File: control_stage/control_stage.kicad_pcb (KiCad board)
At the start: 2 copper layers, 100 x 80 mm, 108 parts, among them J1 DB9, J2 DB15, P1 CONN_01X04, P2 CONN_01X04, P3 CONN_01X04, P4 CONN_01X04, P8 CONN_01X01, U1 XMC4400-F100, U14 AD8226, U15 MAX3463, U18 LT1764EQ, U19 KSZ8081, U2 ips511g, U20 ETH100_MAG, U21 MAX3463, U22 MAX3463, U23 MAX3463, U3 ips511g, U4 MAX3463, U5 AD8226, U6 LT1764EQ, X1 NKE1212DC, Y1 12MHz, Y2 25MHz

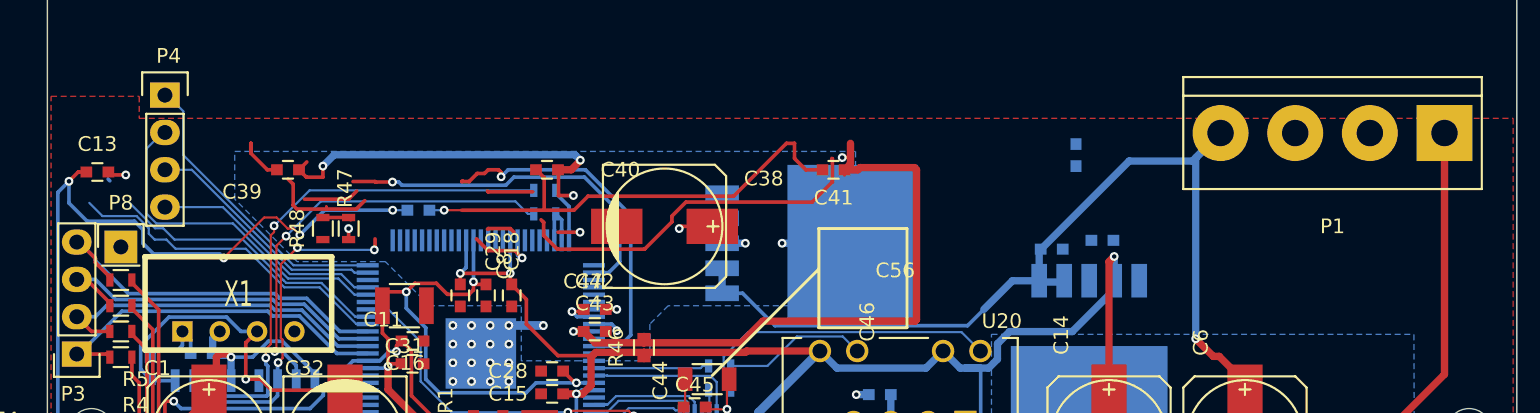
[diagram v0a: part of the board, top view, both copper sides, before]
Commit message: Control stage, initial version.
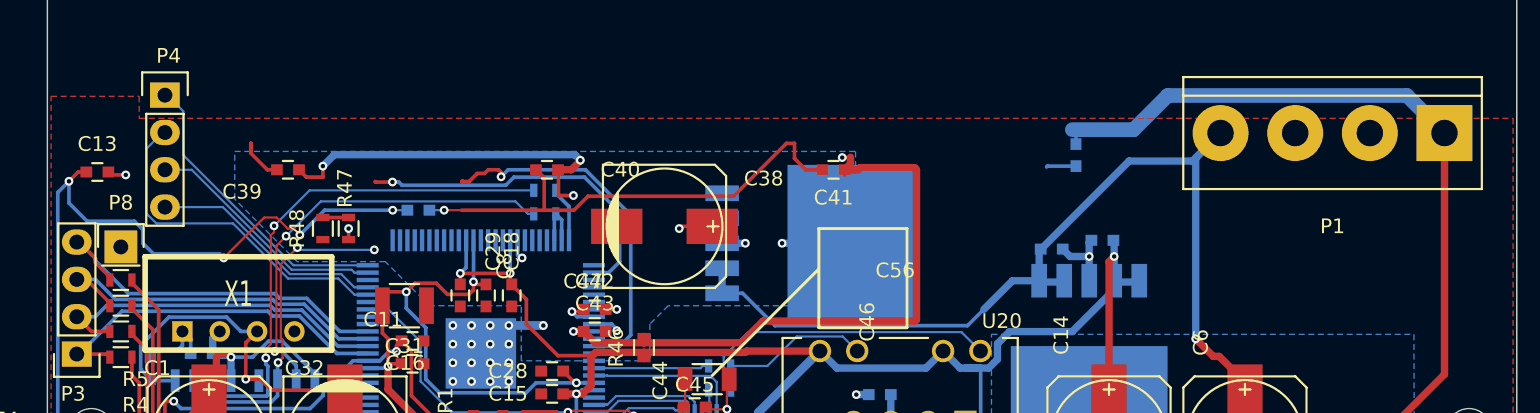
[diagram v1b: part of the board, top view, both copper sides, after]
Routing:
- net +12V: track 157.3 -> 185.7 mm
- net Net-(U13-Pad7): track 24.9 -> 0.00 mm
- net /MCLK: track 22.6 -> 0.00 mm
- net /MDAT: track 19.4 -> 0.00 mm
- net Net-(U11-Pad7): track 7.35 -> 0.00 mm
- net GND: track 159.8 -> 166.7 mm, vias 38 -> 39
- net Net-(R6-Pad2): track 3.78 -> 0.00 mm
- net /CUR2: track 5.03 -> 1.39 mm
- net +3.3VADC: track 78.1 -> 74.9 mm, vias 9 -> 8
- net Net-(R10-Pad2): track 3.10 -> 0.00 mm
- net +3.3V: track 216.8 -> 219.6 mm
- net Net-(R12-Pad2): track 1.92 -> 0.00 mm
- net /CUR0: track 24.9 -> 23.4 mm
- net Net-(U14-Pad6): track 24.5 -> 23.8 mm
